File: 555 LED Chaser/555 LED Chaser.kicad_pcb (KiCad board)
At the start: 2 copper layers, 85.1 x 41.9 mm, 20 parts, among them J1 Barrel_Jack, U1 LM555, U2 4017

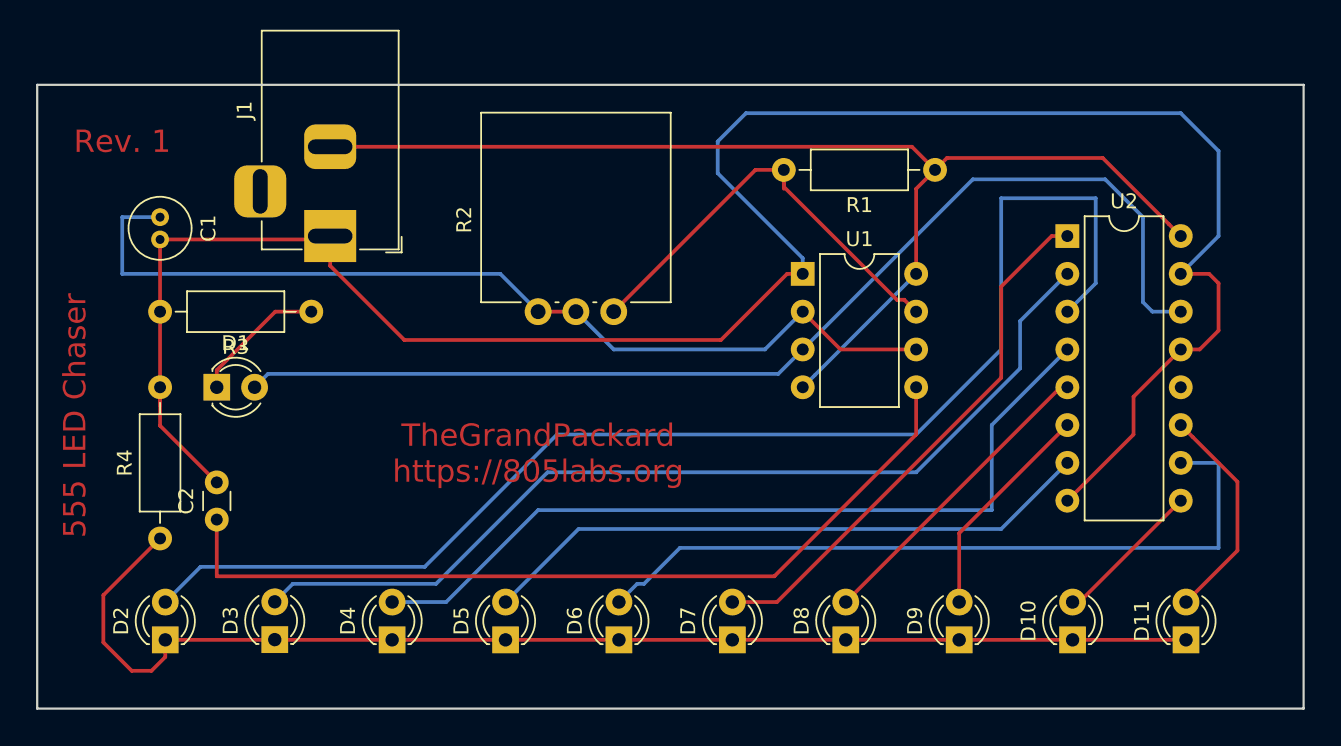
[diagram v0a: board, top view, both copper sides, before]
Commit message: Modified traces to be 1mm wide for better vinyl printing
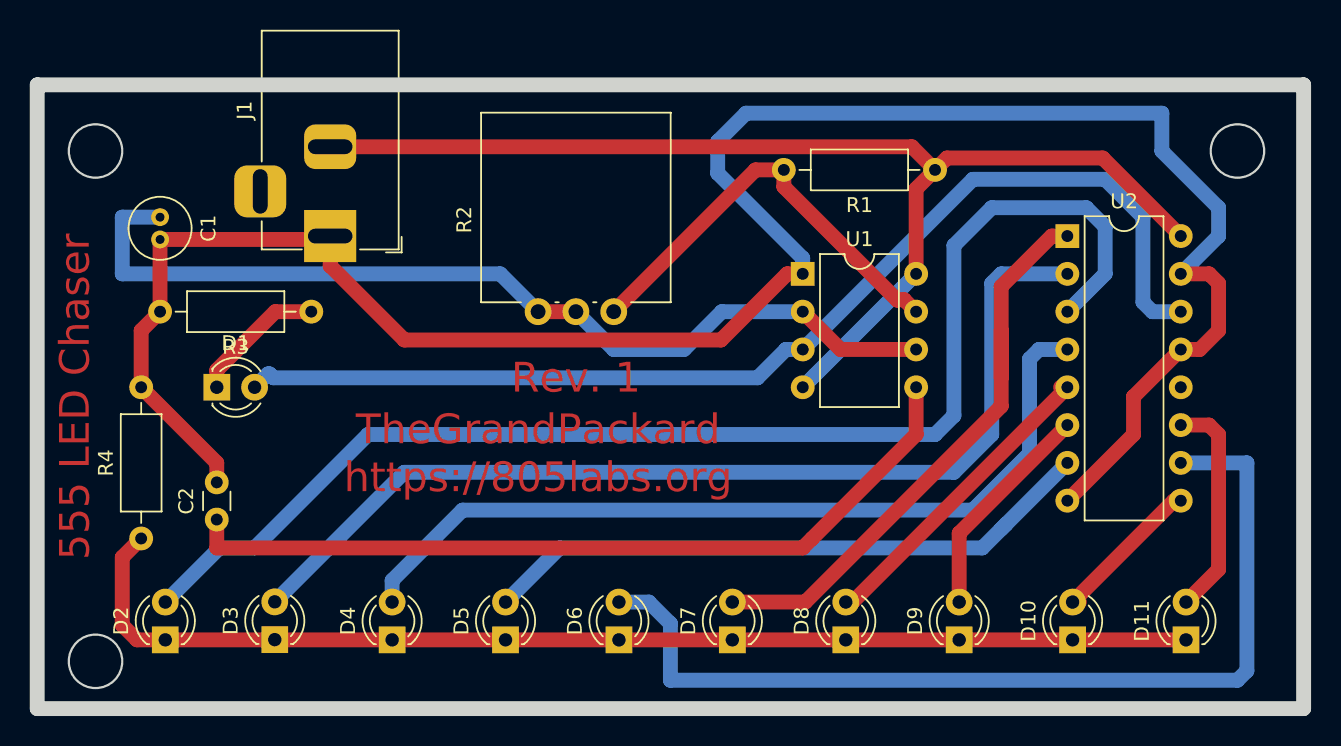
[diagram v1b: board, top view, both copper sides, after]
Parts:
- C2: value 0.01μ -> 0.01μF
- moved R4 1.27 mm to (116.8, 140.3)
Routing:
- net Net-(D6-Pad2): track 50.0 -> 65.3 mm
- net Net-(D10-Pad1): track 83.6 -> 78.2 mm
- net Net-(D7-Pad2): track 36.3 -> 40.6 mm
- net Net-(D3-Pad2): track 64.2 -> 68.3 mm
- net Net-(C2-Pad1): track 57.9 -> 55.2 mm
- net Net-(R1-Pad2): track 30.2 -> 28.9 mm
- net Net-(D4-Pad2): track 55.7 -> 57.0 mm
- net Net-(C1-Pad2): track 146.7 -> 145.8 mm
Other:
- outline, holes or cut-outs redrawn
- net class Default: trace_width 0.25 -> 1
- rule trace_min: 0.4 -> 1

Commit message: Updated pcb layout
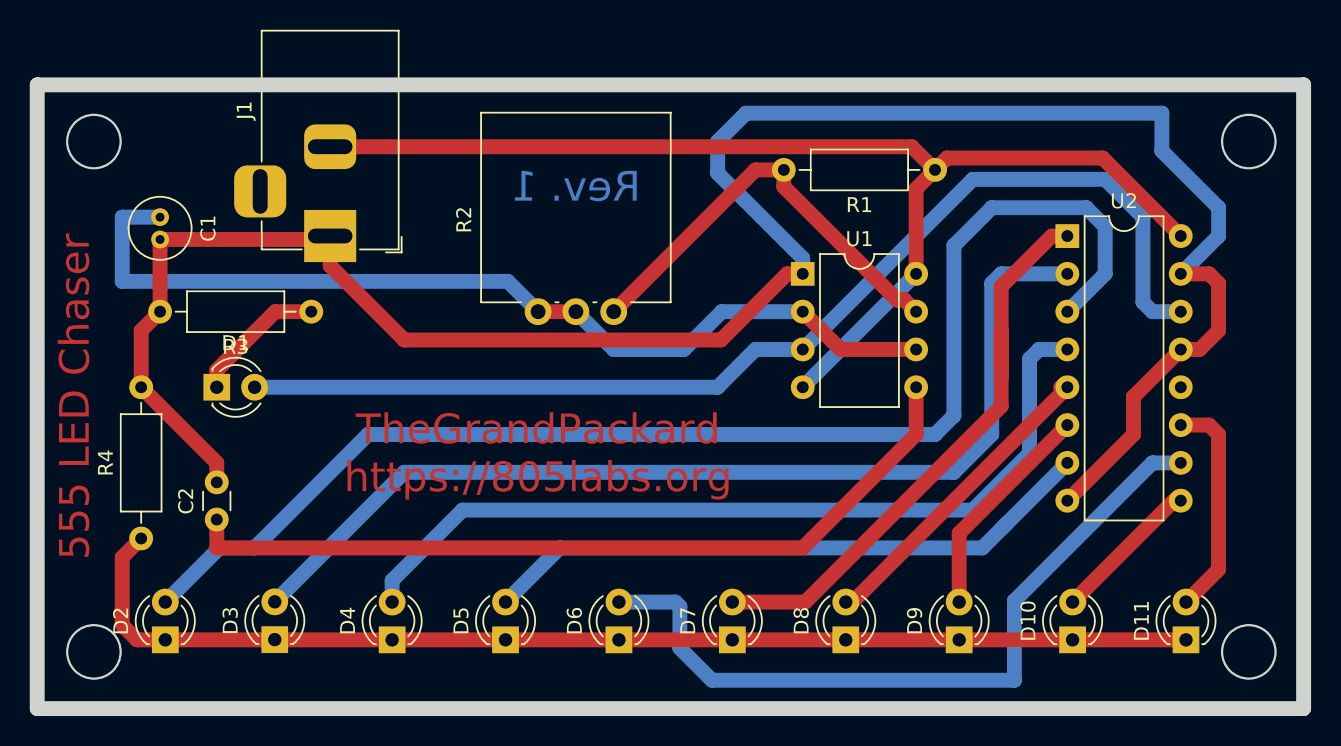
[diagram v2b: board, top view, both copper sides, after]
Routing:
- net Net-(D6-Pad2): track 65.3 -> 50.7 mm
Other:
- outline, holes or cut-outs redrawn
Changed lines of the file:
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@@
   (general
     (thickness 1.6)
-    (drawings 10)
-    (tracks 136)
+    (drawings 11)
+    (tracks 134)
     (zones 0)
     (modules 20)
@@
     (solder_mask_min_width 0.25)
     (aux_axis_origin 0 0)
-    (visible_elements 7FFFFFFF)
+    (visible_elements 7FFFEFFF)
     (pcbplotparams
-      (layerselection 0x00000_fffffffe)
+      (layerselection 0x01000_ffffffff)
       (usegerberextensions false)
       (usegerberattributes false)
       (usegerberadvancedattributes false)
       (creategerberjobfile false)
-      (excludeedgelayer true)
+      (excludeedgelayer false)
       (linewidth 0.100000)
       (plotframeref false)
@@
       (plotvalue false)
       (plotinvisibletext false)
-      (padsonsilk false)
+      (padsonsilk true)
       (subtractmaskfromsilk false)
-      (outputformat 4)
-      (mirror true)
+      (outputformat 3)
+      (mirror false)
       (drillshape 0)
       (scaleselection 1)
@@
     )
   )
-  (gr_circle (center 113.773949 148.59) (end 115.57 148.59) (layer Edge.Cuts) (width 0.15))
-  (gr_circle (center 113.773949 114.3) (end 115.57 114.3) (layer Edge.Cuts) (width 0.15))
-  (gr_circle (center 190.5 114.3) (end 192.296051 114.3) (layer Edge.Cuts) (width 0.15))
+  (gr_circle (center 191.262 147.955) (end 193.058051 147.955) (layer Edge.Cuts) (width 0.15))
+  (gr_circle (center 113.665 147.955) (end 115.461051 147.955) (layer Edge.Cuts) (width 0.15))
+  (gr_circle (center 113.665 113.665) (end 115.461051 113.665) (layer Edge.Cuts) (width 0.15))
+  (gr_circle (center 191.262 113.665) (end 193.058051 113.665) (layer Edge.Cuts) (width 0.15))
   (gr_line (start 109.855 151.765) (end 109.855 109.855) (layer Edge.Cuts) (width 1))
   (gr_line (start 194.945 151.765) (end 109.855 151.765) (layer Edge.Cuts) (width 1))
@@
     (effects (font (size 2 2) (thickness 0.3)))
   )
-  (gr_text "Rev. 1" (at 146.05 129.54) (layer F.Cu)
-    (effects (font (size 2 2) (thickness 0.3)))
+  (gr_text "Rev. 1" (at 146.05 116.713) (layer B.Cu)
+    (effects (font (size 2 2) (thickness 0.3)) (justify mirror))
   )
   (gr_text "555 LED Chaser" (at 112.395 130.81 90) (layer F.Cu)
@@
   (segment (start 163.83 127.635) (end 168.91 127.635) (width 1) (layer F.Cu) (net 1))
   (segment (start 161.29 125.095) (end 163.83 127.635) (width 1) (layer F.Cu) (net 1))
-  (segment (start 115.57 118.745) (end 118.11 118.745) (width 1) (layer B.Cu) (net 1))
-  (segment (start 115.57 122.555) (end 115.57 118.745) (width 1) (layer B.Cu) (net 1))
-  (segment (start 143.51 125.095) (end 140.97 122.555) (width 1) (layer B.Cu) (net 1))
-  (segment (start 140.97 122.555) (end 115.57 122.555) (width 1) (layer B.Cu) (net 1))
   (segment (start 155.85226 125.095) (end 161.29 125.095) (width 1) (layer B.Cu) (net 1))
   (segment (start 153.31226 127.635) (end 155.85226 125.095) (width 1) (layer B.Cu) (net 1))
   (segment (start 146.05 125.095) (end 148.59 127.635) (width 1) (layer B.Cu) (net 1))
   (segment (start 148.59 127.635) (end 153.31226 127.635) (width 1) (layer B.Cu) (net 1))
+  (segment (start 141.478 123.063) (end 143.51 125.095) (width 1) (layer B.Cu) (net 1))
+  (segment (start 115.57 123.063) (end 141.478 123.063) (width 1) (layer B.Cu) (net 1))
+  (segment (start 118.11 118.745) (end 115.57 118.745) (width 1) (layer B.Cu) (net 1))
+  (segment (start 115.57 118.745) (end 115.57 123.063) (width 1) (layer B.Cu) (net 1))
   (segment (start 118.11 125.095) (end 118.11 120.245) (width 1) (layer F.Cu) (net 2))
   (segment (start 129.31 120.245) (end 129.54 120.015) (width 1) (layer F.Cu) (net 2))
@@
   (segment (start 161.29 127.635) (end 172.72 116.205) (width 1) (layer B.Cu) (net 4))
   (segment (start 172.72 116.205) (end 181.61 116.205) (width 1) (layer B.Cu) (net 4))
-  (segment (start 160.15863 127.635) (end 158.25363 129.54) (width 1) (layer B.Cu) (net 4))
-  (segment (start 161.29 127.635) (end 160.15863 127.635) (width 1) (layer B.Cu) (net 4))
-  (segment (start 158.25363 129.54) (end 125.73 129.54) (width 1) (layer B.Cu) (net 4))
-  (segment (start 125.359999 129.275001) (end 124.46 130.175) (width 1) (layer B.Cu) (net 4))
-  (segment (start 125.465001 129.275001) (end 125.359999 129.275001) (width 1) (layer B.Cu) (net 4))
-  (segment (start 125.73 129.54) (end 125.465001 129.275001) (width 1) (layer B.Cu) (net 4))
+  (segment (start 158.115 127.635) (end 161.29 127.635) (width 1) (layer B.Cu) (net 4))
+  (segment (start 124.46 130.175) (end 155.575 130.175) (width 1) (layer B.Cu) (net 4))
+  (segment (start 155.575 130.175) (end 158.115 127.635) (width 1) (layer B.Cu) (net 4))
   (segment (start 121.92 130.175) (end 121.92 129.025) (width 1) (layer F.Cu) (net 5))
   (segment (start 125.85 125.095) (end 128.27 125.095) (width 1) (layer F.Cu) (net 5))
@@
   (segment (start 174.625 139.7) (end 174.9425 139.3825) (width 1) (layer B.Cu) (net 10))
   (segment (start 174.9425 139.3825) (end 179.07 135.255) (width 1) (layer B.Cu) (net 10))
-  (segment (start 150.956596 144.606596) (end 148.941431 144.606596) (width 1) (layer B.Cu) (net 11))
-  (segment (start 191.135 135.255) (end 191.135 149.225) (width 1) (layer B.Cu) (net 11))
-  (segment (start 186.69 135.255) (end 191.135 135.255) (width 1) (layer B.Cu) (net 11))
-  (segment (start 191.135 149.225) (end 190.5 149.86) (width 1) (layer B.Cu) (net 11))
-  (segment (start 190.5 149.86) (end 152.4 149.86) (width 1) (layer B.Cu) (net 11))
-  (segment (start 152.4 149.86) (end 152.4 146.05) (width 1) (layer B.Cu) (net 11))
-  (segment (start 152.4 146.05) (end 150.956596 144.606596) (width 1) (layer B.Cu) (net 11))
+  (segment (start 152.734596 144.606596) (end 148.941431 144.606596) (width 1) (layer B.Cu) (net 11))
+  (segment (start 153.035 144.907) (end 152.734596 144.606596) (width 1) (layer B.Cu) (net 11))
+  (segment (start 184.785 135.255) (end 175.514 144.526) (width 1) (layer B.Cu) (net 11))
+  (segment (start 186.69 135.255) (end 184.785 135.255) (width 1) (layer B.Cu) (net 11))
+  (segment (start 175.514 144.526) (end 175.514 149.86) (width 1) (layer B.Cu) (net 11))
+  (segment (start 175.514 149.86) (end 155.194 149.86) (width 1) (layer B.Cu) (net 11))
+  (segment (start 155.194 149.86) (end 153.035 147.701) (width 1) (layer B.Cu) (net 11))
+  (segment (start 153.035 147.701) (end 153.035 144.907) (width 1) (layer B.Cu) (net 11))
   (segment (start 178.02 120.015) (end 179.07 120.015) (width 1) (layer F.Cu) (net 12))
   (segment (start 174.625 123.41) (end 178.02 120.015) (width 1) (layer F.Cu) (net 12))

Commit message: Final tweaks before submitting to fabrication
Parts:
- removed J1: Barrel_Jack, Connector_BarrelJack:BarrelJack_Horizontal
- removed R2: 10k, Potentiometer_THT:Potentiometer_Vishay_148-149_Single_Vertical
- removed R4: 680, Resistor_THT:R_Axial_DIN0207_L6.3mm_D2.5mm_P10.16mm_Horizontal
- added 10k: 10k, Potentiometer_THT:Potentiometer_Vishay_148-149_Single_Vertical, F.Cu at (148.6, 125.1)
- added 3-12V DC: 5-9V DC, Connector_BarrelJack:BarrelJack_Horizontal, F.Cu at (129.5, 120.0)
- added 680: 680, Resistor_THT:R_Axial_DIN0207_L6.3mm_D2.5mm_P10.16mm_Horizontal, F.Cu at (116.8, 140.3)
- 1: renamed from D2; value LED -> 1
- 10: renamed from D11; value LED -> 10
- 2: renamed from D3; value LED -> 2
- 3: renamed from D4; value LED -> 3
- 4: renamed from D5; value LED -> 4
- 5: renamed from D6; value LED -> 5
- 555: renamed from U1; value LM555 -> 555
- 6: renamed from D7; value LED -> 6
- 7: renamed from D8; value LED -> 7
- 8: renamed from D9; value LED -> 8
- 9: renamed from D10; value LED -> 9
- CLOCK: renamed from D1; value LED -> CLOCK
- renumbered C2 to 0.01μF, R1 to 10k, C1 to 10μF, U2 to 4017, R3 to 680
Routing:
- net Net-(C1-Pad2): track 145.8 -> 115.9 mm, vias 0 -> 4
- net Net-(D2-Pad2): track 88.1 -> 68.7 mm
- net Net-(D5-Pad2): track 42.1 -> 52.2 mm
- net Net-(J1-Pad2): track 78.6 -> 88.1 mm, vias 0 -> 3
- net Net-(D6-Pad2): track 50.7 -> 42.7 mm
- net Net-(C1-Pad1): track 64.2 -> 56.7 mm
- net Net-(D1-Pad2): track 75.0 -> 68.3 mm
- net Net-(D7-Pad2): track 40.6 -> 45.4 mm, vias 0 -> 2
- net Net-(D4-Pad2): track 57.0 -> 52.4 mm
- net Net-(C2-Pad1): track 55.2 -> 50.8 mm
- net Net-(D3-Pad2): track 68.3 -> 65.8 mm
- net Net-(D11-Pad2): track 15.0 -> 16.7 mm
- net Net-(D10-Pad2): track 10.5 -> 12.2 mm
- net Net-(R1-Pad2): track 28.9 -> 29.8 mm
- net Net-(D10-Pad1): track 78.2 -> 77.7 mm
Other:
- outline, holes or cut-outs redrawn
- net class Default: trace_width 1 -> 0.25; via_dia 0.8 -> 0.6; via_drill 0.4 -> 0.3
- rule trace_min: 1 -> 0.25
- rule via_min_size: 0.4 -> 0.25
